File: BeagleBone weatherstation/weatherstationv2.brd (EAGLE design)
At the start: 86.4 x 54.6 mm, 11 parts, among them P1 CONN23-2F, P2 CONN23-2FB

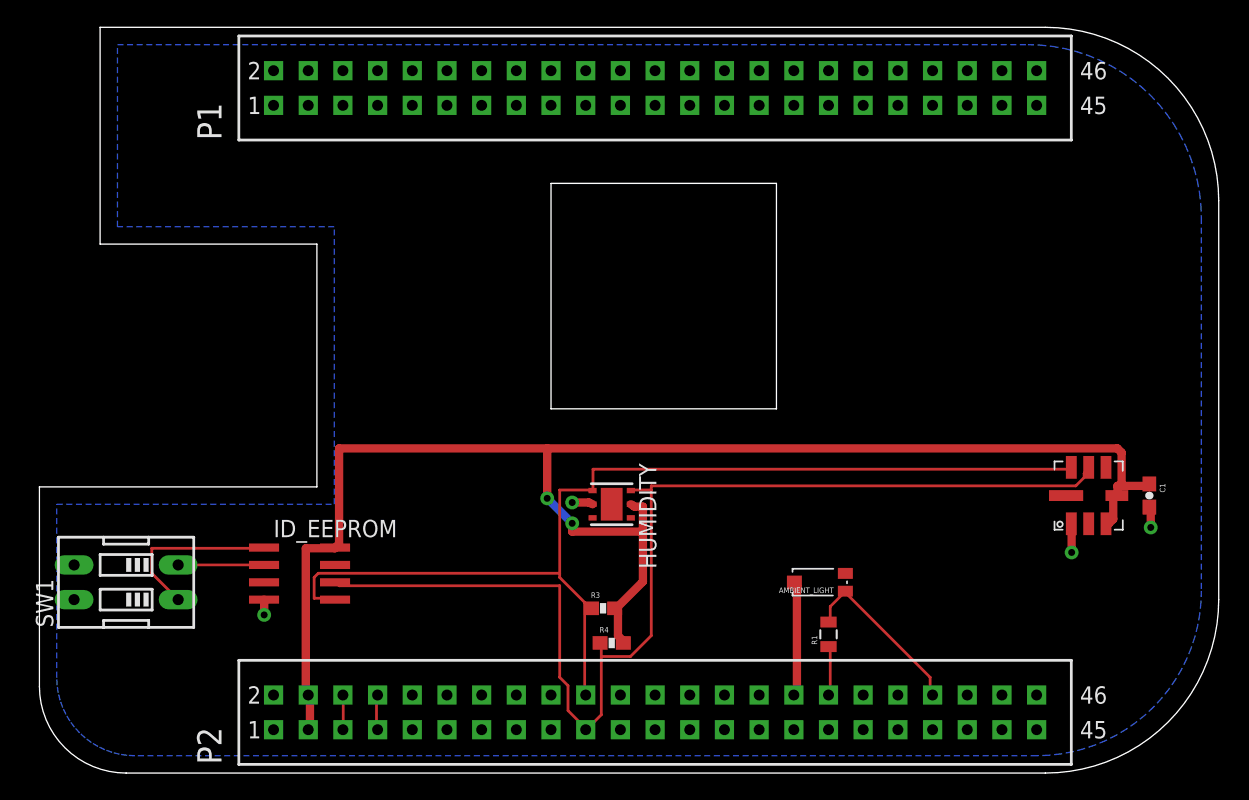
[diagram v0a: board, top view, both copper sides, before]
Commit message: weatherstation: update silkscreen
Signed-off-by: Koen Kooi <koen@dominion.thruhere.net>
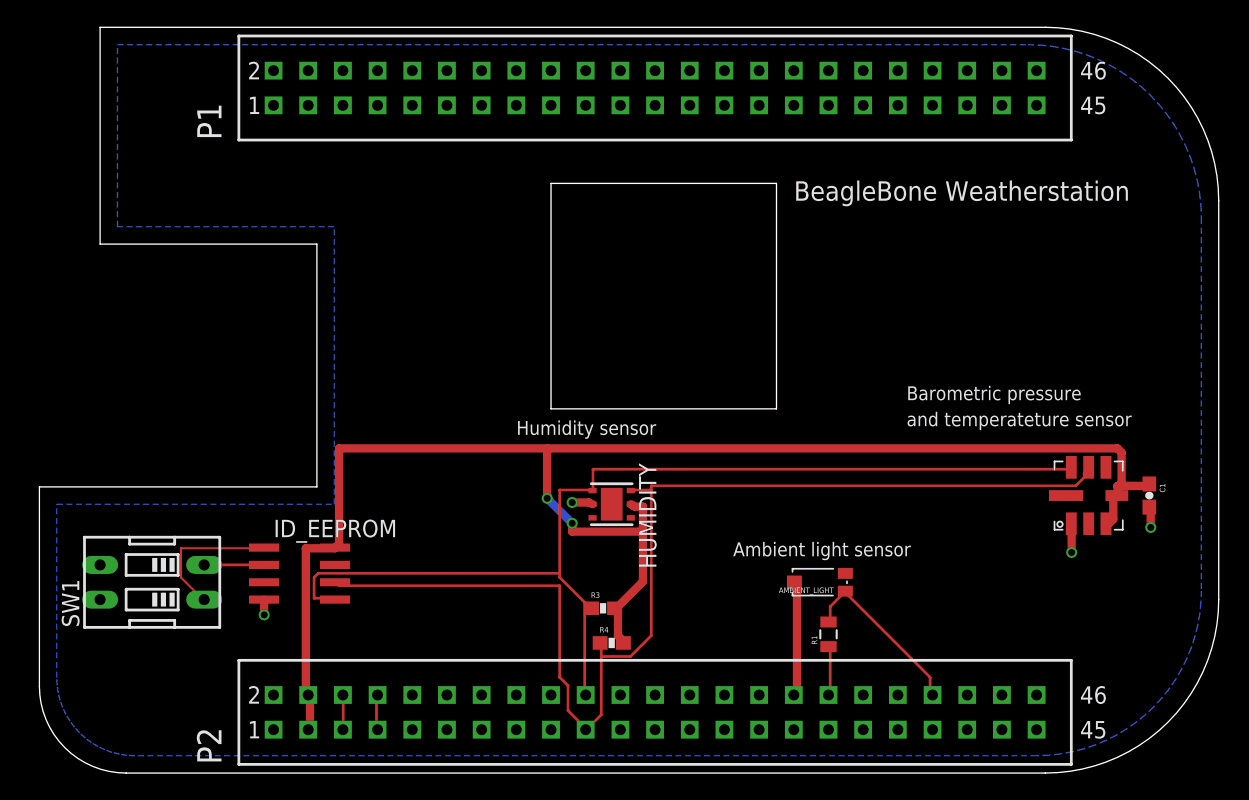
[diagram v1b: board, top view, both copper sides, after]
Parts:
- moved SW1 1.91 mm to (8.26, 14.0)
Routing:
- net N$1: track 12.8 -> 10.6 mm
- net N$7: track 6.29 -> 4.38 mm
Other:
- board text added: "Ambient light sensor"
- board text added: "Barometric pressure"
- board text added: "BeagleBone Weatherstation"
- board text added: "Humidity sensor"
- board text added: "and temperateture sensor"
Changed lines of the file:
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@@
 <layer number="19" name="Unrouted" color="6" fill="1" visible="yes" active="yes"/>
 <layer number="20" name="Dimension" color="15" fill="1" visible="yes" active="yes"/>
-<layer number="21" name="tPlace" color="7" fill="1" visible="yes" active="yes"/>
+<layer number="21" name="tPlace" color="12" fill="1" visible="yes" active="yes"/>
 <layer number="22" name="bPlace" color="7" fill="1" visible="yes" active="yes"/>
 <layer number="23" name="tOrigins" color="15" fill="1" visible="yes" active="yes"/>
@@
 <layer number="49" name="Reference" color="7" fill="1" visible="yes" active="yes"/>
 <layer number="50" name="dxf" color="7" fill="1" visible="yes" active="yes"/>
-<layer number="51" name="tDocu" color="7" fill="1" visible="yes" active="yes"/>
+<layer number="51" name="tDocu" color="14" fill="1" visible="yes" active="yes"/>
 <layer number="52" name="bDocu" color="7" fill="1" visible="yes" active="yes"/>
 <layer number="53" name="tGND_GNDA" color="7" fill="9" visible="no" active="no"/>
@@
 <text x="76.2" y="5.08" size="1.27" layer="21">46</text>
 <text x="76.2" y="50.8" size="1.27" layer="21">46</text>
+<text x="50.8" y="15.875" size="1.016" layer="21">Ambient light sensor</text>
+<text x="63.5" y="27.305" size="1.016" layer="21">Barometric pressure</text>
+<text x="63.5" y="25.4" size="1.016" layer="21">and temperateture sensor</text>
+<text x="55.245" y="41.91" size="1.4224" layer="21" font="vector">BeagleBone Weatherstation</text>
+<text x="34.925" y="24.765" size="1.016" layer="21" font="vector">Humidity sensor</text>
 </plain>
 <attributes>
@@
 </classes>
 <designrules>
+<description language="de">&lt;b&gt;EAGLE Design Rules&lt;/b&gt;
+&lt;p&gt;
+Die Standard-Design-Rules sind so gewählt, dass sie für
+die meisten Anwendungen passen. Sollte ihre Platine
+besondere Anforderungen haben, treffen Sie die erforderlichen
+Einstellungen hier und speichern die Design Rules unter
+einem neuen Namen ab.</description>
 <description language="en">&lt;b&gt;EAGLE Design Rules&lt;/b&gt;
 &lt;p&gt;
@@
 may have different requirements, so please make the
 necessary adjustments and save your customized
-design rules under a new name.
+design rules under a new name.</description>
+<description language="zh">&lt;b&gt;Seeed Studio EAGLE Design Rules&lt;/b&gt;
 </description>
-<description language="nl">&lt;b&gt;EAGLE Design Rules&lt;/b&gt;
-&lt;p&gt;
-The default Design Rules have been set to cover
-a wide range of applications. Your particular design
-may have different requirements, so please make the
-necessary adjustments and save your customized
-design rules under a new name.</description>
 <param name="layerSetup" value="(1*16)"/>
 <param name="mtCopper" value="0.035mm 0.035mm 0.035mm 0.035mm 0.035mm 0.035mm 0.035mm 0.035mm 0.035mm 0.035mm 0.035mm 0.035mm 0.035mm 0.035mm 0.035mm 0.035mm"/>
 <param name="mtIsolate" value="1.5mm 0.15mm 0.2mm 0.15mm 0.2mm 0.15mm 0.2mm 0.15mm 0.2mm 0.15mm 0.2mm 0.15mm 0.2mm 0.15mm 0.2mm"/>
-<param name="mdWireWire" value="8mil"/>
-<param name="mdWirePad" value="8mil"/>
-<param name="mdWireVia" value="8mil"/>
-<param name="mdPadPad" value="8mil"/>
-<param name="mdPadVia" value="8mil"/>
-<param name="mdViaVia" value="8mil"/>
-<param name="mdSmdPad" value="8mil"/>
-<param name="mdSmdVia" value="8mil"/>
-<param name="mdSmdSmd" value="8mil"/>
+<param name="mdWireWire" value="6mil"/>
+<param name="mdWirePad" value="6mil"/>
+<param name="mdWireVia" value="6mil"/>
+<param name="mdPadPad" value="6mil"/>
+<param name="mdPadVia" value="6mil"/>
+<param name="mdViaVia" value="6mil"/>
+<param name="mdSmdPad" value="0mil"/>
+<param name="mdSmdVia" value="0mil"/>
+<param name="mdSmdSmd" value="0mil"/>
 <param name="mdViaViaSameLayer" value="8mil"/>
 <param name="mnLayersViaInSmd" value="2"/>
 <param name="mdCopperDimension" value="10mil"/>
-<param name="mdDrill" value="8mil"/>
+<param name="mdDrill" value="10mil"/>
 <param name="mdSmdStop" value="0mil"/>
-<param name="msWidth" value="8mil"/>
-<param name="msDrill" value="20mil"/>
-<param name="msMicroVia" value="9.99mm"/>
+<param name="msWidth" value="6mil"/>
+<param name="msDrill" value="12mil"/>
+<param name="msMicroVia" value="12mil"/>
 <param name="msBlindViaRatio" value="0.5"/>
 <param name="rvPadTop" value="0.25"/>
@@
 <param name="rvMicroViaOuter" value="0.25"/>
 <param name="rvMicroViaInner" value="0.25"/>
-<param name="rlMinPadTop" value="12mil"/>
+<param name="rlMinPadTop" value="10mil"/>
 <param name="rlMaxPadTop" value="20mil"/>
 <param name="rlMinPadInner" value="10mil"/>
 <param name="rlMaxPadInner" value="20mil"/>
-<param name="rlMinPadBottom" value="12mil"/>
+<param name="rlMinPadBottom" value="10mil"/>
 <param name="rlMaxPadBottom" value="20mil"/>
-<param name="rlMinViaOuter" value="10mil"/>
+<param name="rlMinViaOuter" value="6mil"/>
 <param name="rlMaxViaOuter" value="20mil"/>
-<param name="rlMinViaInner" value="10mil"/>
+<param name="rlMinViaInner" value="6mil"/>
 <param name="rlMaxViaInner" value="20mil"/>
 <param name="rlMinMicroViaOuter" value="4mil"/>
@@
 <param name="psTop" value="-1"/>
 <param name="psBottom" value="-1"/>
-<param name="psFirst" value="-1"/>
+<param name="psFirst" value="0"/>
 <param name="psElongationLong" value="100"/>
 <param name="psElongationOffset" value="100"/>
 <param name="mvStopFrame" value="1"/>
 <param name="mvCreamFrame" value="0"/>
-<param name="mlMinStopFrame" value="4mil"/>
-<param name="mlMaxStopFrame" value="4mil"/>
+<param name="mlMinStopFrame" value="2mil"/>
+<param name="mlMaxStopFrame" value="2mil"/>
 <param name="mlMinCreamFrame" value="0mil"/>
 <param name="mlMaxCreamFrame" value="0mil"/>
-<param name="mlViaStopLimit" value="25mil"/>
+<param name="mlViaStopLimit" value="100mil"/>
 <param name="srRoundness" value="0"/>
 <param name="srMinRoundness" value="0mil"/>
@@
 <param name="checkAngle" value="0"/>
 <param name="checkFont" value="1"/>
-<param name="checkRestrict" value="1"/>
+<param name="checkRestrict" value="0"/>
 <param name="useDiameter" value="13"/>
 <param name="maxErrors" value="50"/>
@@
 <attribute name="OC_NEWARK" value="27C9144" x="19.05" y="14.605" size="1.778" layer="27" rot="R270" display="off"/>
 </element>
-<element name="SW1" library="SparkFun" package="DIPSWITCH-02" value="" x="6.35" y="13.97" rot="R90"/>
+<element name="SW1" library="SparkFun" package="DIPSWITCH-02" value="" x="8.255" y="13.97" rot="R90"/>
 </elements>
 <signals>
@@
 <contactref element="ID_EEPROM" pad="2"/>
 <contactref element="SW1" pad="2"/>
-<wire x1="10.16" y1="15.24" x2="16.45" y2="15.24" width="0.2032" layer="1"/>
+<wire x1="12.065" y1="15.24" x2="16.45" y2="15.24" width="0.2032" layer="1"/>
 </signal>
 <signal name="N$1">
 <contactref element="SW1" pad="1"/>
 <contactref element="ID_EEPROM" pad="1"/>
-<wire x1="8.2296" y1="16.4592" x2="16.1544" y2="16.4592" width="0.2032" layer="1"/>
-<wire x1="8.2296" y1="14.6304" x2="8.2296" y2="16.4592" width="0.2032" layer="1"/>
-<wire x1="10.16" y1="12.7" x2="8.2296" y2="14.6304" width="0.2032" layer="1"/>
 <wire x1="16.1544" y1="16.4592" x2="16.45" y2="16.51" width="0.2032" layer="1"/>
+<wire x1="10.3632" y1="16.4592" x2="16.1544" y2="16.4592" width="0.1524" layer="1"/>
+<wire x1="10.3632" y1="14.3256" x2="10.3632" y2="16.4592" width="0.1524" layer="1"/>
+<wire x1="11.8872" y1="12.8016" x2="10.3632" y2="14.3256" width="0.1524" layer="1"/>
+<wire x1="11.8872" y1="12.8016" x2="12.065" y2="12.7" width="0.1524" layer="1"/>
 </signal>
 </signals>

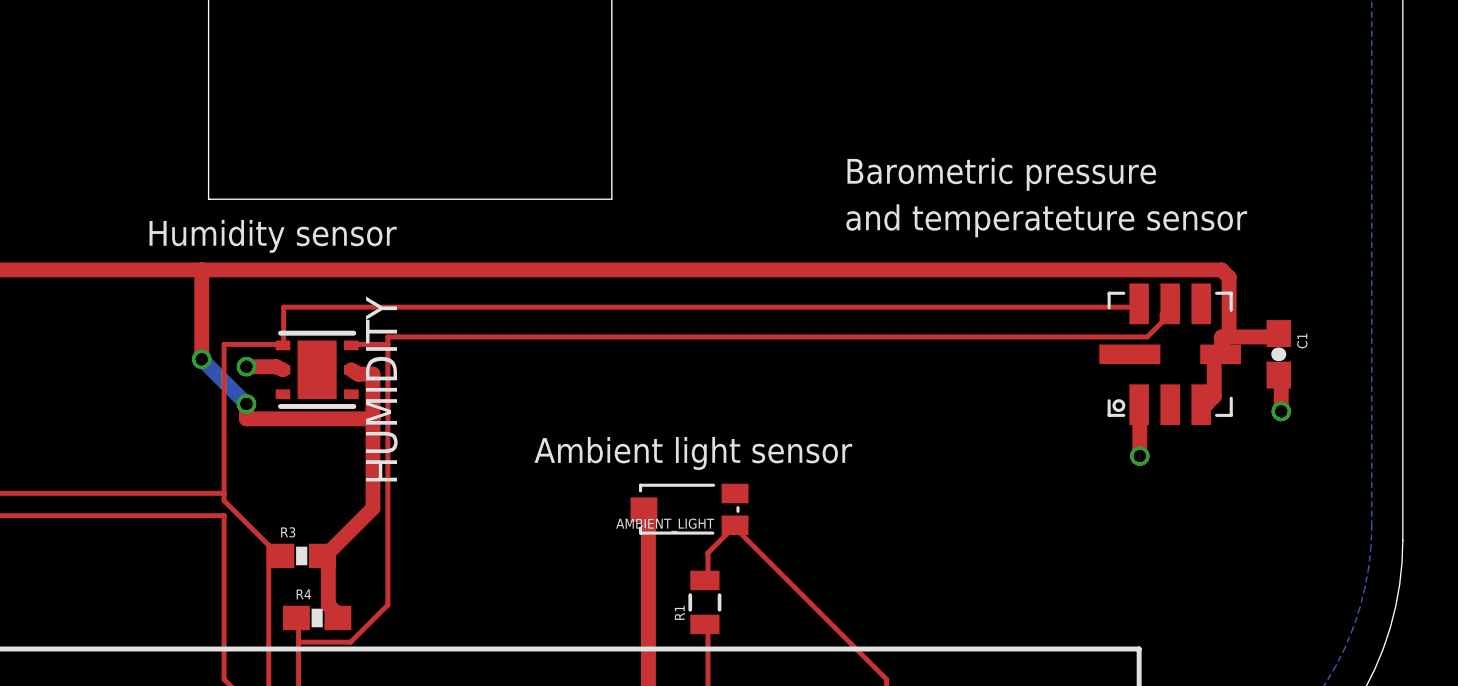
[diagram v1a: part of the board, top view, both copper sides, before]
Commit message: weatherstation: add eagleUP attributes
Signed-off-by: Koen Kooi <koen@dominion.thruhere.net>
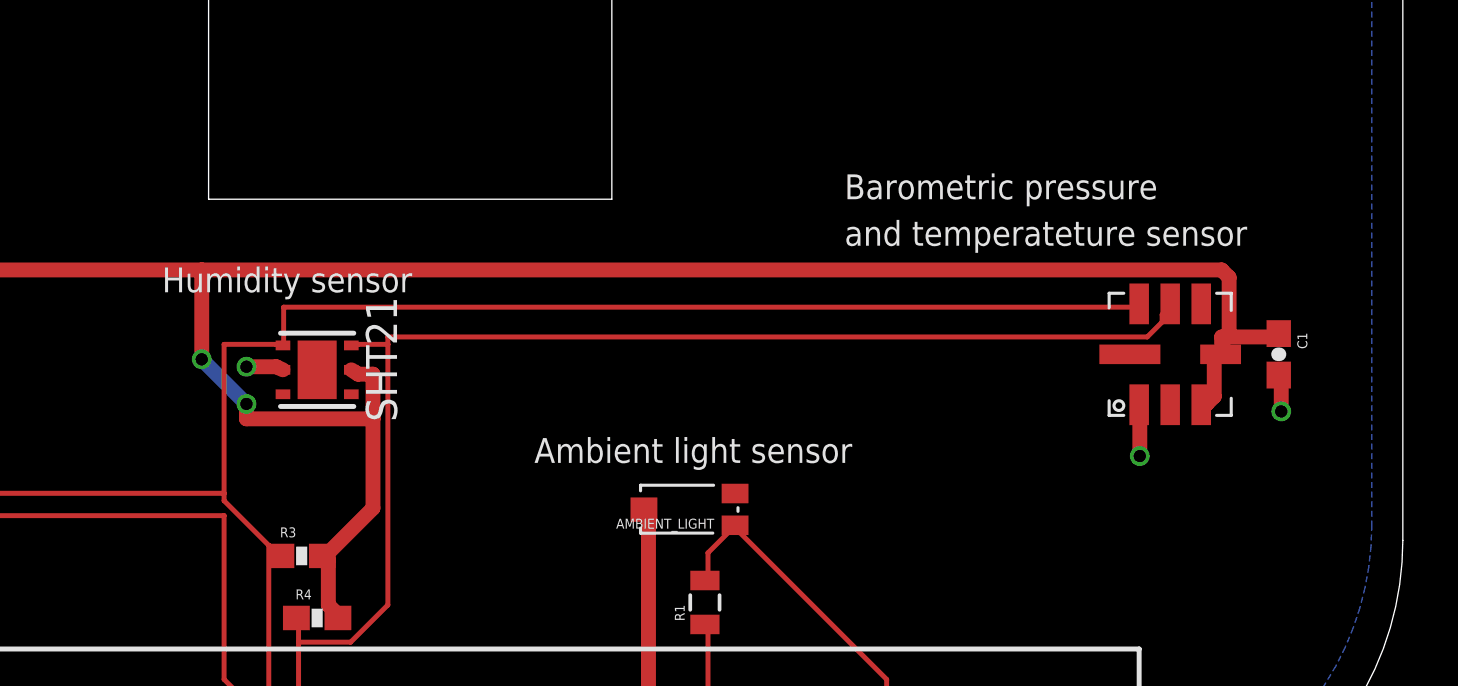
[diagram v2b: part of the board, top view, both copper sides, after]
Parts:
- renumbered HUMIDITY to SHT21
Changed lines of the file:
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@@
 <setting verticaltext="up"/>
 </settings>
-<grid distance="0.025" unitdist="inch" unit="inch" style="lines" multiple="1" display="yes" altdistance="0.025" altunitdist="inch" altunit="inch"/>
+<grid distance="0.025" unitdist="inch" unit="mm" style="lines" multiple="1" display="yes" altdistance="0.025" altunitdist="inch" altunit="inch"/>
 <layers>
 <layer number="1" name="Top" color="4" fill="1" visible="yes" active="yes"/>
@@
 <layer number="106" name="bPlate" color="7" fill="1" visible="yes" active="yes"/>
 <layer number="107" name="Crop" color="7" fill="1" visible="yes" active="yes"/>
-<layer number="116" name="Patch_BOT" color="9" fill="4" visible="yes" active="yes"/>
 <layer number="121" name="_tsilk" color="7" fill="1" visible="yes" active="yes"/>
 <layer number="122" name="_bsilk" color="7" fill="1" visible="yes" active="yes"/>
@@
 <layer number="220" name="220bmp" color="21" fill="1" visible="no" active="no"/>
 <layer number="221" name="221bmp" color="22" fill="1" visible="no" active="no"/>
-<layer number="222" name="222bmp" color="23" fill="1" visible="no" active="no"/>
 <layer number="223" name="223bmp" color="24" fill="1" visible="no" active="no"/>
 <layer number="224" name="224bmp" color="25" fill="1" visible="no" active="no"/>
@@
 <text x="76.2" y="50.8" size="1.27" layer="21">46</text>
 <text x="50.8" y="15.875" size="1.016" layer="21">Ambient light sensor</text>
-<text x="63.5" y="27.305" size="1.016" layer="21">Barometric pressure</text>
-<text x="63.5" y="25.4" size="1.016" layer="21">and temperateture sensor</text>
+<text x="63.5" y="26.67" size="1.016" layer="21">Barometric pressure</text>
+<text x="63.5" y="24.765" size="1.016" layer="21">and temperateture sensor</text>
 <text x="55.245" y="41.91" size="1.4224" layer="21" font="vector">BeagleBone Weatherstation</text>
-<text x="34.925" y="24.765" size="1.016" layer="21" font="vector">Humidity sensor</text>
+<text x="35.56" y="22.86" size="1.016" layer="21" font="vector">Humidity sensor</text>
 </plain>
 <attributes>
@@
 </autorouter>
 <elements>
-<element name="P1" library="conn23-2f" package="CONN23-2F" value="CONN23-2F" x="45.085" y="50.165" rot="R90"/>
-<element name="P2" library="conn23-2f" package="CONN23-2F" value="CONN23-2FB" x="45.085" y="4.445" rot="R90"/>
+<element name="P1" library="conn23-2f" package="CONN23-2F" value="CONN23-2F" x="45.085" y="50.165" rot="R90">
+<attribute name="EAGLEUP" value="CONN23-2F;MR90" x="45.085" y="50.165" size="1.778" layer="27" rot="R90" display="off"/>
+</element>
+<element name="P2" library="conn23-2f" package="CONN23-2F" value="CONN23-2FB" x="45.085" y="4.445" rot="R90">
+<attribute name="EAGLEUP" value="CONN23-2F;MR90" x="45.085" y="4.445" size="1.778" layer="27" rot="R90" display="off"/>
+</element>
 <element name="BAROMETRIC_PRESSURE" library="SparkFun" package="BMP085" value="BMP085" x="76.835" y="20.32" rot="R90"/>
 <element name="C1" library="SparkFun" package="0603-CAP" value="100nF" x="81.28" y="20.32" rot="R270"/>
@@
 <element name="R4" library="SparkFun" package="0603-RES" value="4.7k" x="41.91" y="9.525"/>
 <element name="AMBIENT_LIGHT" library="SparkFun" package="TEMT6000-SEN" value="TEMT6000" x="57.15" y="13.97" rot="R180"/>
-<element name="R1" library="SparkFun" package="0805" value="10k" x="57.785" y="10.16" rot="R90"/>
-<element name="HUMIDITY" library="ALX" package="SHT21" value="SHT2x" x="41.91" y="19.685" rot="R270"/>
+<element name="R1" library="SparkFun" package="0805" value="10k" x="57.785" y="10.16" rot="R90">
+<attribute name="EAGLEUP" value="R0805" x="57.785" y="10.16" size="1.778" layer="27" rot="R90" display="off"/>
+</element>
+<element name="SHT21" library="ALX" package="SHT21" value="SHT2x" x="41.91" y="19.685" rot="R270"/>
 <element name="ID_EEPROM" library="microchip" package="SO-08" value="24LC256SN" x="19.05" y="14.605" rot="R270">
 <attribute name="MF" value="MICROCHIP" x="19.05" y="14.605" size="1.778" layer="27" rot="R270" display="off"/>
@@
 <contactref element="P2" pad="44"/>
 <contactref element="C1" pad="2"/>
-<contactref element="HUMIDITY" pad="2"/>
+<contactref element="SHT21" pad="2"/>
 <contactref element="SW1" pad="3"/>
 <contactref element="SW1" pad="4"/>
@@
 <contactref element="BAROMETRIC_PRESSURE" pad="7"/>
 <contactref element="R3" pad="1"/>
-<contactref element="HUMIDITY" pad="1"/>
+<contactref element="SHT21" pad="1"/>
 <contactref element="ID_EEPROM" pad="5"/>
 <wire x1="38.1" y1="20.7264" x2="40.2336" y2="20.7264" width="0.2032" layer="1"/>
@@
 <contactref element="C1" pad="1"/>
 <contactref element="BAROMETRIC_PRESSURE" pad="4"/>
-<contactref element="HUMIDITY" pad="5"/>
+<contactref element="SHT21" pad="5"/>
 <contactref element="ID_EEPROM" pad="8"/>
 <wire x1="44.196" y1="19.5072" x2="43.5864" y2="19.5072" width="0.6096" layer="1"/>
@@
 <contactref element="BAROMETRIC_PRESSURE" pad="6"/>
 <contactref element="R4" pad="1"/>
-<contactref element="HUMIDITY" pad="6"/>
+<contactref element="SHT21" pad="6"/>
 <contactref element="ID_EEPROM" pad="6"/>
 <wire x1="38.1" y1="13.716" x2="21.9456" y2="13.716" width="0.2032" layer="1"/>
